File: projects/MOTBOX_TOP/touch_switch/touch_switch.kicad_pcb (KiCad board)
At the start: 2 copper layers, 10 x 15 mm, 3 parts, among them J1 Conn_01x03, J2 Conn_01x04

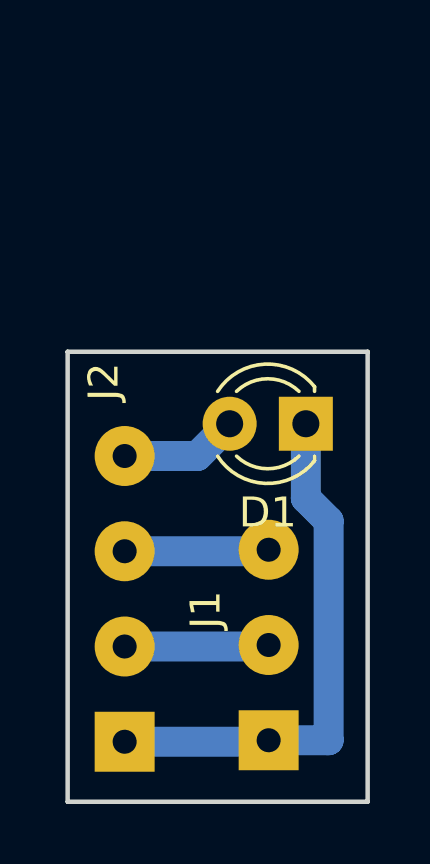
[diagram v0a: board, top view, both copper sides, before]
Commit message: New library files and schematics with ESE31 and DT045 switches
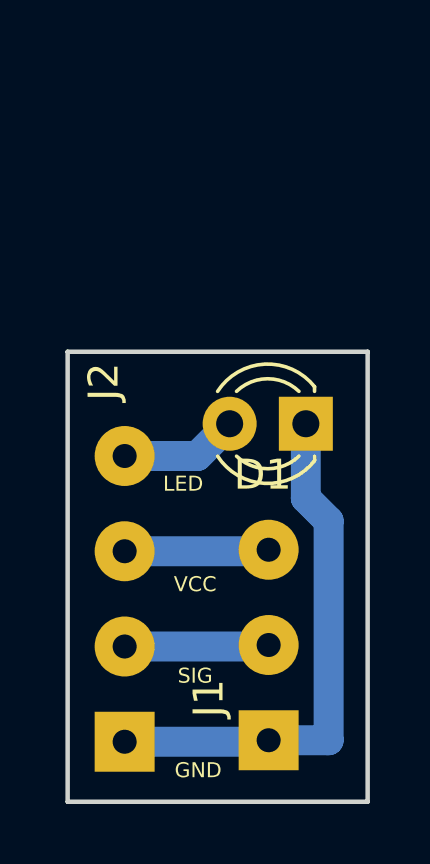
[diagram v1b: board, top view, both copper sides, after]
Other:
- board text added: "GND"
- board text added: "LED"
- board text added: "SIG"
- board text added: "VCC"
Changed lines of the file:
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@@
   (general
     (thickness 1.6)
-    (drawings 4)
+    (drawings 8)
     (tracks 12)
     (zones 0)
@@
     (uvia_min_size 0.2)
     (uvia_min_drill 0.1)
-    (pcb_text_width 0.3)
-    (pcb_text_size 1.5 1.5)
+    (pcb_text_width 0.05)
+    (pcb_text_size 0.5 0.5)
     (mod_edge_width 0.15)
     (mod_text_size 1 1)
@@
     (visible_elements FFFFFF7F)
     (pcbplotparams
-      (layerselection 0x010fc_ffffffff)
+      (layerselection 0x010fc_fffffffe)
       (usegerberextensions true)
       (usegerberattributes false)
@@
     (tags connector)
     (attr virtual)
-    (fp_text reference J1 (at 4.35 -2.1 90) (layer F.SilkS)
+    (fp_text reference J1 (at 1.4 -2 90) (layer F.SilkS)
       (effects (font (size 1 1) (thickness 0.15)))
     )
@@
     (descr "LED, diameter 3.0mm, 2 pins")
     (tags "LED diameter 3.0mm 2 pins")
-    (fp_text reference D1 (at 1.27 -2.96 180) (layer F.SilkS)
+    (fp_text reference D1 (at 1.44 -1.7 180) (layer F.SilkS)
       (effects (font (size 1 1) (thickness 0.15)))
     )
@@
     )
   )
+  (gr_text LED (at 134.85 69) (layer F.SilkS)
+    (effects (font (size 0.5 0.5) (thickness 0.05)))
+  )
+  (gr_text SIG (at 135.25 75.4) (layer F.SilkS)
+    (effects (font (size 0.5 0.5) (thickness 0.025)))
+  )
+  (gr_text VCC (at 135.25 72.35) (layer F.SilkS)
+    (effects (font (size 0.5 0.5) (thickness 0.025)))
+  )
+  (gr_text GND (at 135.35 78.55) (layer F.SilkS)
+    (effects (font (size 0.5 0.5) (thickness 0.025)))
+  )
   (gr_line (start 141 79.6) (end 141 64.6) (layer Edge.Cuts) (width 0.15))

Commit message: Touch switch with feedback light changes
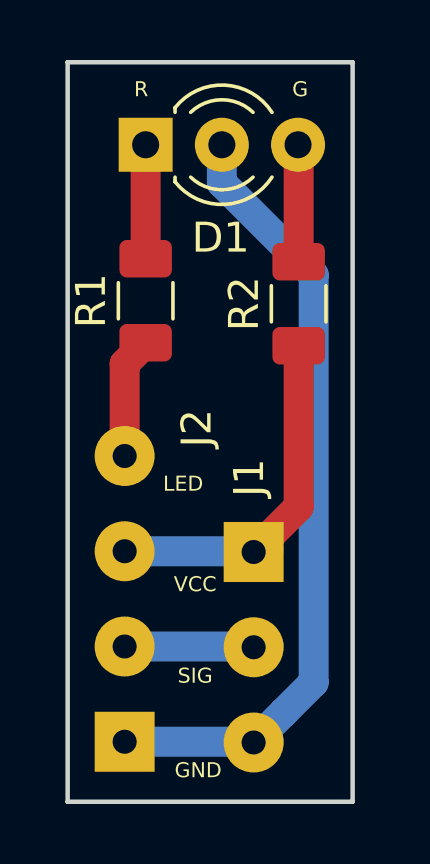
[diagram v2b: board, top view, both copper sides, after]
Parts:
- added R1: 150R, Resistor_SMD:R_1206_3216Metric, F.Cu at (133.6, 62.9)
- added R2: 150R, Resistor_SMD:R_1206_3216Metric, F.Cu at (138.7, 63.0)
- D1: value LED -> LED_Dual_ACA; footprint LED_THT:LED_D3.0mm -> LED_THT:LED_D3.0mm-3
- moved D1 10.7 mm to (133.6, 57.7), turned to 0 degrees
- moved J1 6.29 mm to (137.2, 71.3), turned to 270 degrees
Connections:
- J1 pad 1: Net-(D1-Pad1) -> Net-(J1-Pad1)
- J1 pad 3: Net-(J1-Pad3) -> Net-(D1-Pad2)
- J2 pad 1: Net-(D1-Pad1) -> Net-(D1-Pad2)
- J2 pad 3: Net-(J1-Pad3) -> Net-(J1-Pad1)
- J2 pad 4: Net-(D1-Pad2) -> Net-(J2-Pad4)
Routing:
- net Net-(D1-Pad2): track 3.95 -> 26.4 mm
- net Net-(D1-Pad1): track 17.7 -> 3.80 mm
- net Net-(J1-Pad1): track 0.00 -> 11.9 mm
- net Net-(J1-Pad3): track 4.82 -> 0.00 mm
- net Net-(J2-Pad4): track 0.00 -> 4.06 mm
- net Net-(D1-Pad3): track 0.00 -> 3.91 mm
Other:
- board size 10 x 15 mm -> 9.5 x 24.6 mm
- board text added: "G"
- board text added: "R"
